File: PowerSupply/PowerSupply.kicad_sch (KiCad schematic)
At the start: 15 parts, among them J1 POWER, J2 VSET, J3 LASER, U0 AL8861Y-13

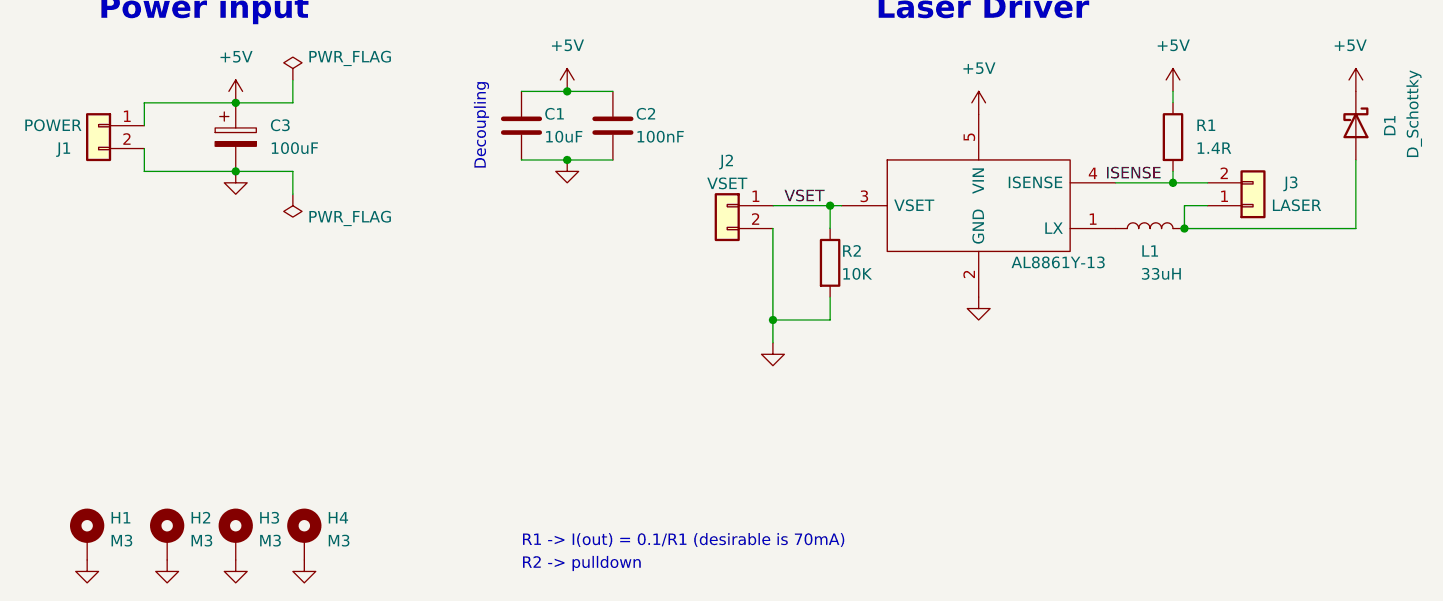
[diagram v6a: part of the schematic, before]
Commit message: Prepare version for manufacturing: finalize PCB layout, add silkscreen
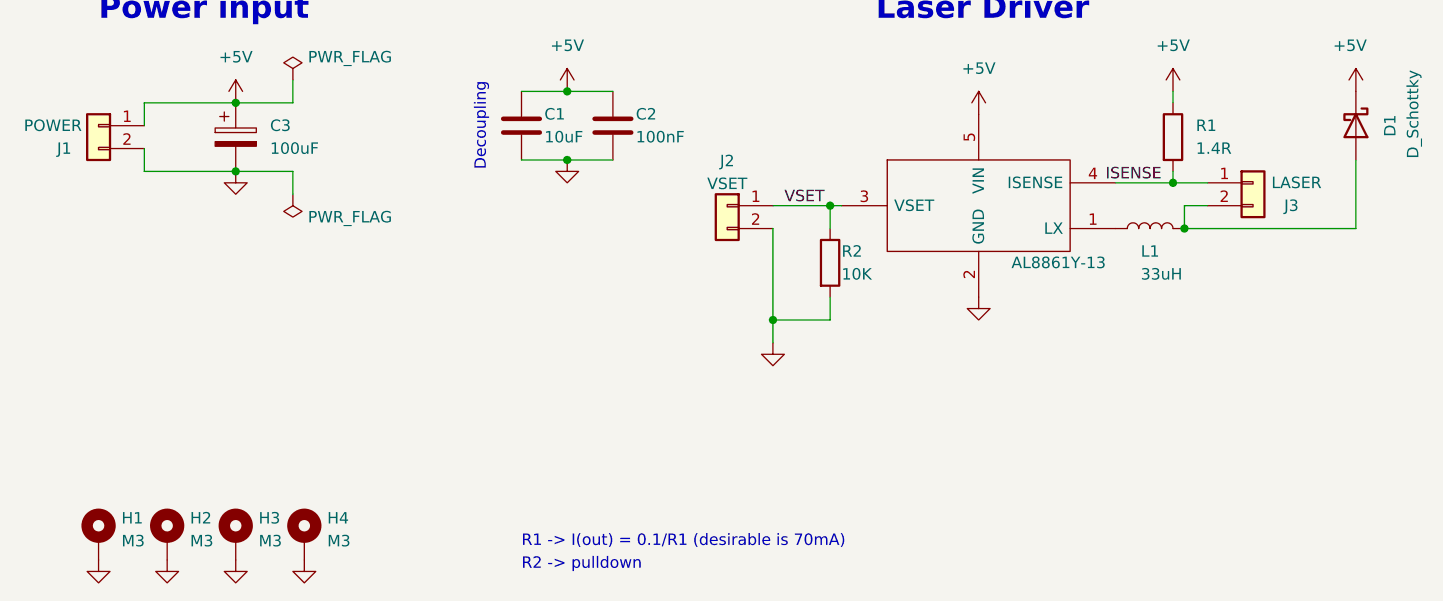
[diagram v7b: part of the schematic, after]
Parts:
- U0: footprint SOT89-5 -> Package_TO_SOT_SMD:SOT-89-5
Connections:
- net ISENSE: now also J3.1 (Pin_1); no longer J3.2 (Pin_2)
- net at D1.2 (A), L1.2: now also J3.2 (Pin_2); no longer J3.1 (Pin_1)
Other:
- moved on the sheet: H1
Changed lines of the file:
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@@
     (effects (font (size 1.27 1.27)) (justify right bottom))
   )
-  (symbol (lib_id "power:GND") (at 63.5 128.27 0) (unit 1)
-    (in_bom yes) (on_board yes) (fields_autoplaced)
-    (property "Reference" "#PWR0111" (id 0) (at 63.5 134.62 0)
-      (effects (font (size 1.27 1.27)) hide)
-    )
-    (property "Value" "GND" (id 1) (at 63.4999 132.08 90)
+  (symbol (lib_id "power:GND") (at 64.77 128.27 0) (unit 1)
+    (in_bom yes) (on_board yes) (fields_autoplaced)
+    (property "Reference" "#PWR0111" (id 0) (at 64.77 134.62 0)
+      (effects (font (size 1.27 1.27)) hide)
+    )
+    (property "Value" "GND" (id 1) (at 64.7699 132.08 90)
       (effects (font (size 1.27 1.27)) (justify right) hide)
     )
-    (property "Footprint" "" (id 2) (at 63.5 128.27 0)
-      (effects (font (size 1.27 1.27)) hide)
-    )
-    (property "Datasheet" "" (id 3) (at 63.5 128.27 0)
+    (property "Footprint" "" (id 2) (at 64.77 128.27 0)
+      (effects (font (size 1.27 1.27)) hide)
+    )
+    (property "Datasheet" "" (id 3) (at 64.77 128.27 0)
       (effects (font (size 1.27 1.27)) hide)
     )
@@
     )
     (property "Value" "AL8861Y-13" (id 1) (at 171.45 95.25 0))
-    (property "Footprint" "SOT89-5" (id 2) (at 162.56 74.93 0)
+    (property "Footprint" "Package_TO_SOT_SMD:SOT-89-5" (id 2) (at 162.56 74.93 0)
       (effects (font (size 1.27 1.27)) (justify left bottom) hide)
     )
@@
     (pin "1")
   )
-  (symbol (lib_id "Mechanical:MountingHole_Pad") (at 63.5 125.73 0) (unit 1)
-    (in_bom yes) (on_board yes) (fields_autoplaced)
-    (property "Reference" "H1" (id 0) (at 66.04 123.6253 0)
-      (effects (font (size 1.27 1.27)) (justify left))
-    )
-    (property "Value" "M3" (id 1) (at 66.04 126.1622 0)
-      (effects (font (size 1.27 1.27)) (justify left))
-    )
-    (property "Footprint" "MountingHole:MountingHole_3.2mm_M3_Pad_Via" (id 2) (at 63.5 125.73 0)
-      (effects (font (size 1.27 1.27)) hide)
-    )
-    (property "Datasheet" "~" (id 3) (at 63.5 125.73 0)
+  (symbol (lib_id "Mechanical:MountingHole_Pad") (at 64.77 125.73 0) (unit 1)
+    (in_bom yes) (on_board yes) (fields_autoplaced)
+    (property "Reference" "H1" (id 0) (at 67.31 123.6253 0)
+      (effects (font (size 1.27 1.27)) (justify left))
+    )
+    (property "Value" "M3" (id 1) (at 67.31 126.1622 0)
+      (effects (font (size 1.27 1.27)) (justify left))
+    )
+    (property "Footprint" "MountingHole:MountingHole_3.2mm_M3_Pad_Via" (id 2) (at 64.77 125.73 0)
+      (effects (font (size 1.27 1.27)) hide)
+    )
+    (property "Datasheet" "~" (id 3) (at 64.77 125.73 0)
       (effects (font (size 1.27 1.27)) hide)
     )
@@
     (pin "1")
   )
-  (symbol (lib_id "Connector_Generic:Conn_01x02") (at 193.04 88.9 0) (mirror x) (unit 1)
-    (in_bom yes) (on_board yes)
-    (property "Reference" "J3" (id 0) (at 198.12 86.36 0)
+  (symbol (lib_id "Connector_Generic:Conn_01x02") (at 193.04 86.36 0) (unit 1)
+    (in_bom yes) (on_board yes)
+    (property "Reference" "J3" (id 0) (at 198.12 88.9 0)
       (effects (font (size 1.27 1.27)) (justify right))
     )
-    (property "Value" "LASER" (id 1) (at 200.66 88.9 0)
+    (property "Value" "LASER" (id 1) (at 200.66 86.36 0)
       (effects (font (size 1.27 1.27)) (justify right))
     )
-    (property "Footprint" "Connector_Molex:Molex_Nano-Fit_105313-xx02_1x02_P2.50mm_Horizontal" (id 2) (at 193.04 88.9 0)
-      (effects (font (size 1.27 1.27)) hide)
-    )
-    (property "Datasheet" "~" (id 3) (at 193.04 88.9 0)
+    (property "Footprint" "Connector_Molex:Molex_Nano-Fit_105313-xx02_1x02_P2.50mm_Horizontal" (id 2) (at 193.04 86.36 0)
+      (effects (font (size 1.27 1.27)) hide)
+    )
+    (property "Datasheet" "~" (id 3) (at 193.04 86.36 0)
       (effects (font (size 1.27 1.27)) hide)
     )
@@
     )
     (path "/31ddefd3-1a8e-42d5-a5b9-a7a71a2b2753"
-      (reference "U0") (unit 1) (value "AL8861Y-13") (footprint "SOT89-5")
-    )
-  )
+      (reference "U0") (unit 1) (value "AL8861Y-13") (footprint "Package_TO_SOT_SMD:SOT-89-5")
+    )
+  )
